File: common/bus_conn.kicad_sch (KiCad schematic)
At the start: 1 part, among them J3 Conn_02x15_Odd_Even

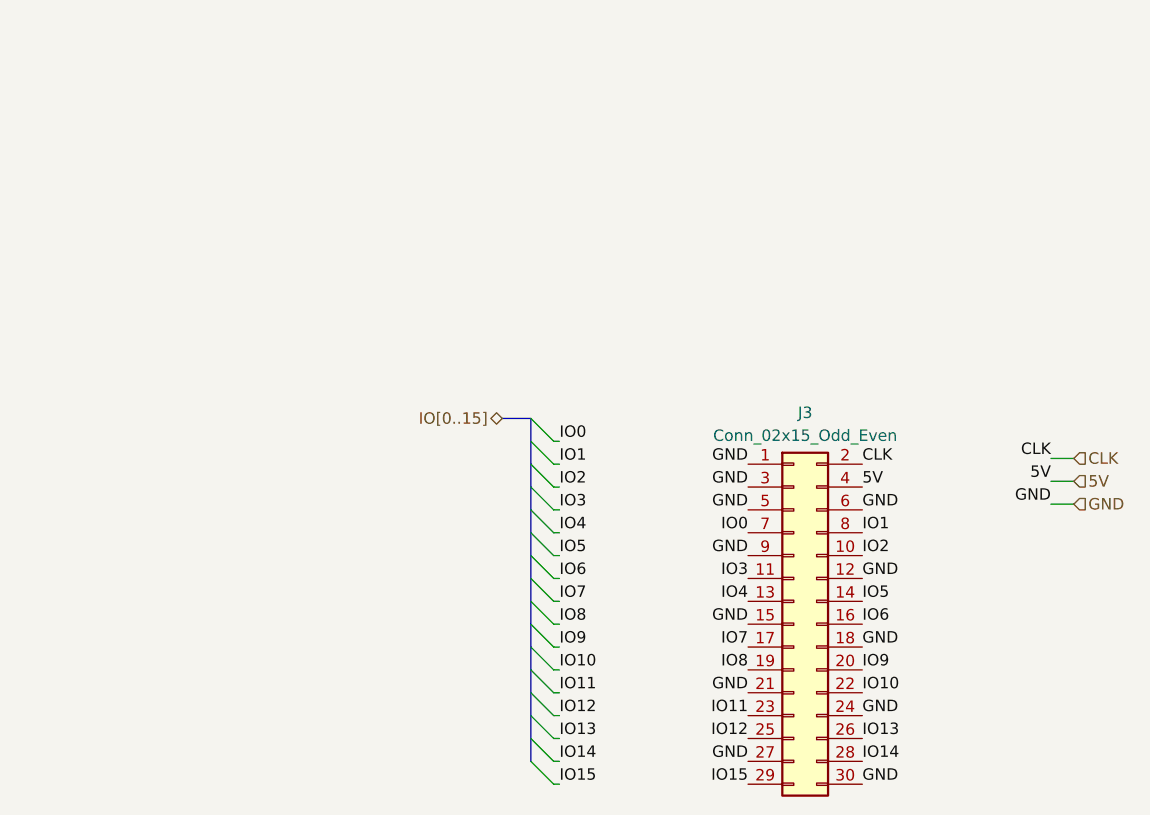
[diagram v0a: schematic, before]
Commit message: Updated ALU and moved common schematics to common/ for enhanced reusability
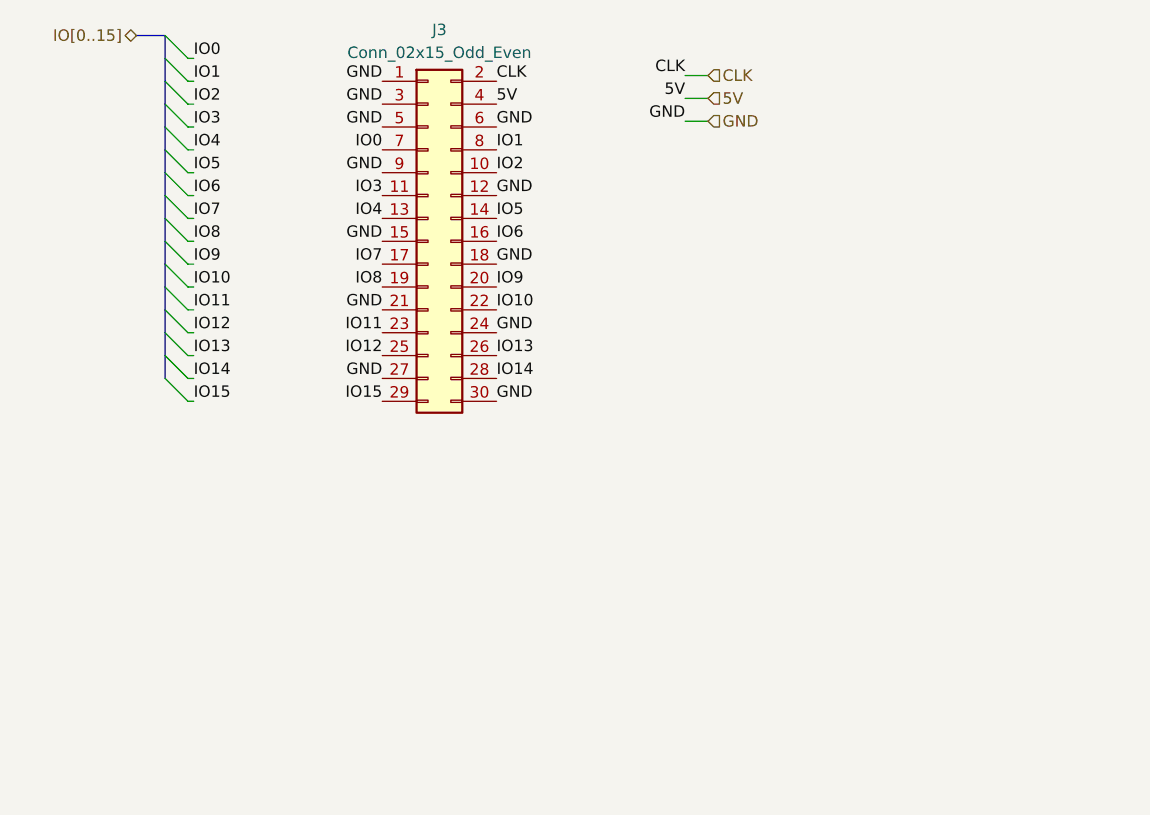
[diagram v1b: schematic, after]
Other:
- title: (none) -> AOS Bus Connector
- moved on the sheet: J3

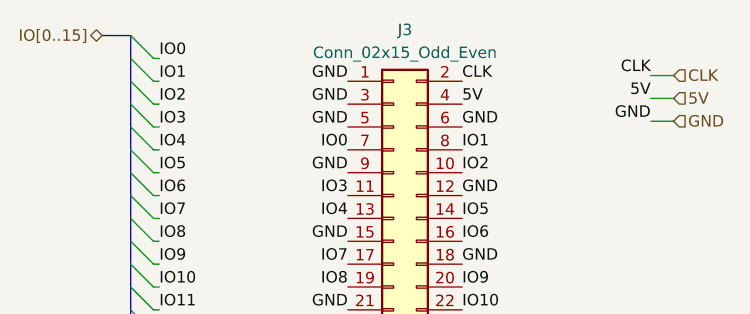
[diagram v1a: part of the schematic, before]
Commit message: Fixed incorrect wiring in ALU (input registers)
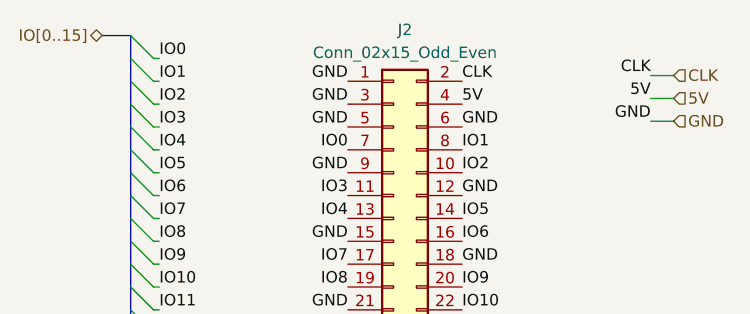
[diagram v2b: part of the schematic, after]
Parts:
- renumbered J3 to J2
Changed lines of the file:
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@@
 (kicad_sch
-	(version 20231120)
+	(version 20250114)
 	(generator "eeschema")
-	(generator_version "8.0")
+	(generator_version "9.0")
 	(paper "A4")
 	(title_block
 		(title "AOS Bus Connector")
 		(date "2025-03-22")
-		(rev "V1.0")
+		(rev "V1.1")
 		(comment 1 "Designed to be used with a 32-pin IDC connector")
 	)
@@
 	(label "IO10"
 		(at 67.31 49.53 0)
-		(fields_autoplaced yes)
 		(effects
 			(font
@@
 	(label "IO5"
 		(at 33.655 34.29 0)
-		(fields_autoplaced yes)
 		(effects
 			(font
@@
 	(label "IO2"
 		(at 33.655 26.67 0)
-		(fields_autoplaced yes)
 		(effects
 			(font
@@
 	(label "IO13"
 		(at 33.655 54.61 0)
-		(fields_autoplaced yes)
 		(effects
 			(font
@@
 	(label "IO3"
 		(at 33.655 29.21 0)
-		(fields_autoplaced yes)
 		(effects
 			(font
@@
 	(label "GND"
 		(at 54.61 24.13 180)
-		(fields_autoplaced yes)
 		(effects
 			(font
@@
 	(label "GND"
 		(at 54.61 41.91 180)
-		(fields_autoplaced yes)
 		(effects
 			(font
@@
 	(label "GND"
 		(at 88.265 28.575 180)
-		(fields_autoplaced yes)
 		(effects
 			(font
@@
 	(label "IO11"
 		(at 33.655 49.53 0)
-		(fields_autoplaced yes)
 		(effects
 			(font
@@
 	(label "5V"
 		(at 88.265 26.035 180)
-		(fields_autoplaced yes)
 		(effects
 			(font
@@
 	(label "IO7"
 		(at 33.655 39.37 0)
-		(fields_autoplaced yes)
 		(effects
 			(font
@@
 	(label "IO10"
 		(at 33.655 46.99 0)
-		(fields_autoplaced yes)
 		(effects
 			(font
@@
 	(label "IO4"
 		(at 33.655 31.75 0)
-		(fields_autoplaced yes)
 		(effects
 			(font
@@
 	(label "IO6"
 		(at 33.655 36.83 0)
-		(fields_autoplaced yes)
 		(effects
 			(font
@@
 	(label "IO4"
 		(at 54.61 39.37 180)
-		(fields_autoplaced yes)
 		(effects
 			(font
@@
 	(label "IO14"
 		(at 33.655 57.15 0)
-		(fields_autoplaced yes)
 		(effects
 			(font
@@
 	(label "IO2"
 		(at 67.31 34.29 0)
-		(fields_autoplaced yes)
 		(effects
 			(font
@@
 	(label "IO11"
 		(at 54.61 52.07 180)
-		(fields_autoplaced yes)
 		(effects
 			(font
@@
 	(label "IO8"
 		(at 33.655 41.91 0)
-		(fields_autoplaced yes)
 		(effects
 			(font
@@
 	(label "GND"
 		(at 67.31 59.69 0)
-		(fields_autoplaced yes)
 		(effects
 			(font
@@
 	(label "IO8"
 		(at 54.61 46.99 180)
-		(fields_autoplaced yes)
 		(effects
 			(font
@@
 	(label "CLK"
 		(at 67.31 24.13 0)
-		(fields_autoplaced yes)
 		(effects
 			(font
@@
 	(label "IO6"
 		(at 67.31 41.91 0)
-		(fields_autoplaced yes)
 		(effects
 			(font
@@
 	(label "IO12"
 		(at 33.655 52.07 0)
-		(fields_autoplaced yes)
 		(effects
 			(font
@@
 	(label "GND"
 		(at 54.61 34.29 180)
-		(fields_autoplaced yes)
 		(effects
 			(font
@@
 	(label "IO1"
 		(at 33.655 24.13 0)
-		(fields_autoplaced yes)
 		(effects
 			(font
@@
 	(label "IO0"
 		(at 54.61 31.75 180)
-		(fields_autoplaced yes)
 		(effects
 			(font
@@
 	(label "GND"
 		(at 54.61 49.53 180)
-		(fields_autoplaced yes)
 		(effects
 			(font
@@
 	(label "IO9"
 		(at 67.31 46.99 0)
-		(fields_autoplaced yes)
 		(effects
 			(font
@@
 	(label "IO3"
 		(at 54.61 36.83 180)
-		(fields_autoplaced yes)
 		(effects
 			(font
@@
 	(label "GND"
 		(at 54.61 26.67 180)
-		(fields_autoplaced yes)
 		(effects
 			(font
@@
 	(label "GND"
 		(at 54.61 29.21 180)
-		(fields_autoplaced yes)
 		(effects
 			(font
@@
 	(label "GND"
 		(at 67.31 29.21 0)
-		(fields_autoplaced yes)
 		(effects
 			(font
@@
 	(label "IO7"
 		(at 54.61 44.45 180)
-		(fields_autoplaced yes)
 		(effects
 			(font
@@
 	(label "5V"
 		(at 67.31 26.67 0)
-		(fields_autoplaced yes)
 		(effects
 			(font
@@
 	(label "IO0"
 		(at 33.655 21.59 0)
-		(fields_autoplaced yes)
 		(effects
 			(font
@@
 	(label "IO15"
 		(at 54.61 59.69 180)
-		(fields_autoplaced yes)
 		(effects
 			(font
@@
 	(label "IO9"
 		(at 33.655 44.45 0)
-		(fields_autoplaced yes)
 		(effects
 			(font
@@
 	(label "GND"
 		(at 54.61 57.15 180)
-		(fields_autoplaced yes)
 		(effects
 			(font
@@
 	(label "IO13"
 		(at 67.31 54.61 0)
-		(fields_autoplaced yes)
 		(effects
 			(font
@@
 	(label "IO15"
 		(at 33.655 59.69 0)
-		(fields_autoplaced yes)
 		(effects
 			(font
@@
 	(label "IO5"
 		(at 67.31 39.37 0)
-		(fields_autoplaced yes)
 		(effects
 			(font
@@
 	(label "CLK"
 		(at 88.265 23.495 180)
-		(fields_autoplaced yes)
 		(effects
 			(font
@@
 	(label "GND"
 		(at 67.31 52.07 0)
-		(fields_autoplaced yes)
 		(effects
 			(font
@@
 	(label "IO1"
 		(at 67.31 31.75 0)
-		(fields_autoplaced yes)
 		(effects
 			(font
@@
 	(label "IO14"
 		(at 67.31 57.15 0)
-		(fields_autoplaced yes)
 		(effects
 			(font
@@
 	(label "GND"
 		(at 67.31 44.45 0)
-		(fields_autoplaced yes)
 		(effects
 			(font
@@
 	(label "IO12"
 		(at 54.61 54.61 180)
-		(fields_autoplaced yes)
 		(effects
 			(font
@@
 	(label "GND"
 		(at 67.31 36.83 0)
-		(fields_autoplaced yes)
 		(effects
 			(font
@@
 		(shape input)
 		(at 90.805 26.035 0)
-		(fields_autoplaced yes)
 		(effects
 			(font
@@
 		(shape input)
 		(at 90.805 23.495 0)
-		(fields_autoplaced yes)
 		(effects
 			(font
@@
 		(shape tri_state)
 		(at 27.305 19.05 180)
-		(fields_autoplaced yes)
 		(effects
 			(font
@@
 		(shape input)
 		(at 90.805 28.575 0)
-		(fields_autoplaced yes)
 		(effects
 			(font
@@
 		(dnp no)
 		(fields_autoplaced yes)
-		(property "Reference" "J3"
+		(property "Reference" "J2"
 			(at 60.96 18.415 0)
 			(effects

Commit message: Refactored files, finalized reg4x16, and used lowercase v
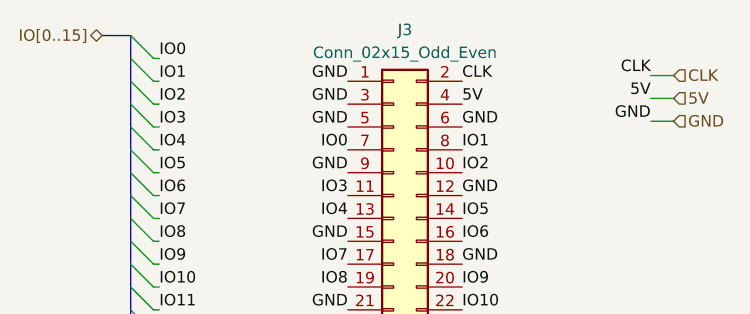
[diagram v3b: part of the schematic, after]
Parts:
- renumbered J2 to J3
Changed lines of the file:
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@@
 		(dnp no)
 		(fields_autoplaced yes)
-		(property "Reference" "J2"
+		(property "Reference" "J3"
 			(at 60.96 18.415 0)
 			(effects
@@
 		)
 		(instances
+			(project "reg4x16"
+				(path "/af77a583-757b-4cb3-a1ea-fa2a5568a329/1c38704f-fad9-48eb-80d8-771b91c8e7ce"
+					(reference "J3")
+					(unit 1)
+				)
+			)
 			(project "ALU"
 				(path "/c0bb03ae-ed0c-4e9e-9f7c-15f29fb8b868/bdad24a6-397c-42d5-914a-4a0f0d69aaaa"
